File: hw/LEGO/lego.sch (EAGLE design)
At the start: 24 parts, among them IC1 ATMEGA48/88/168-AU

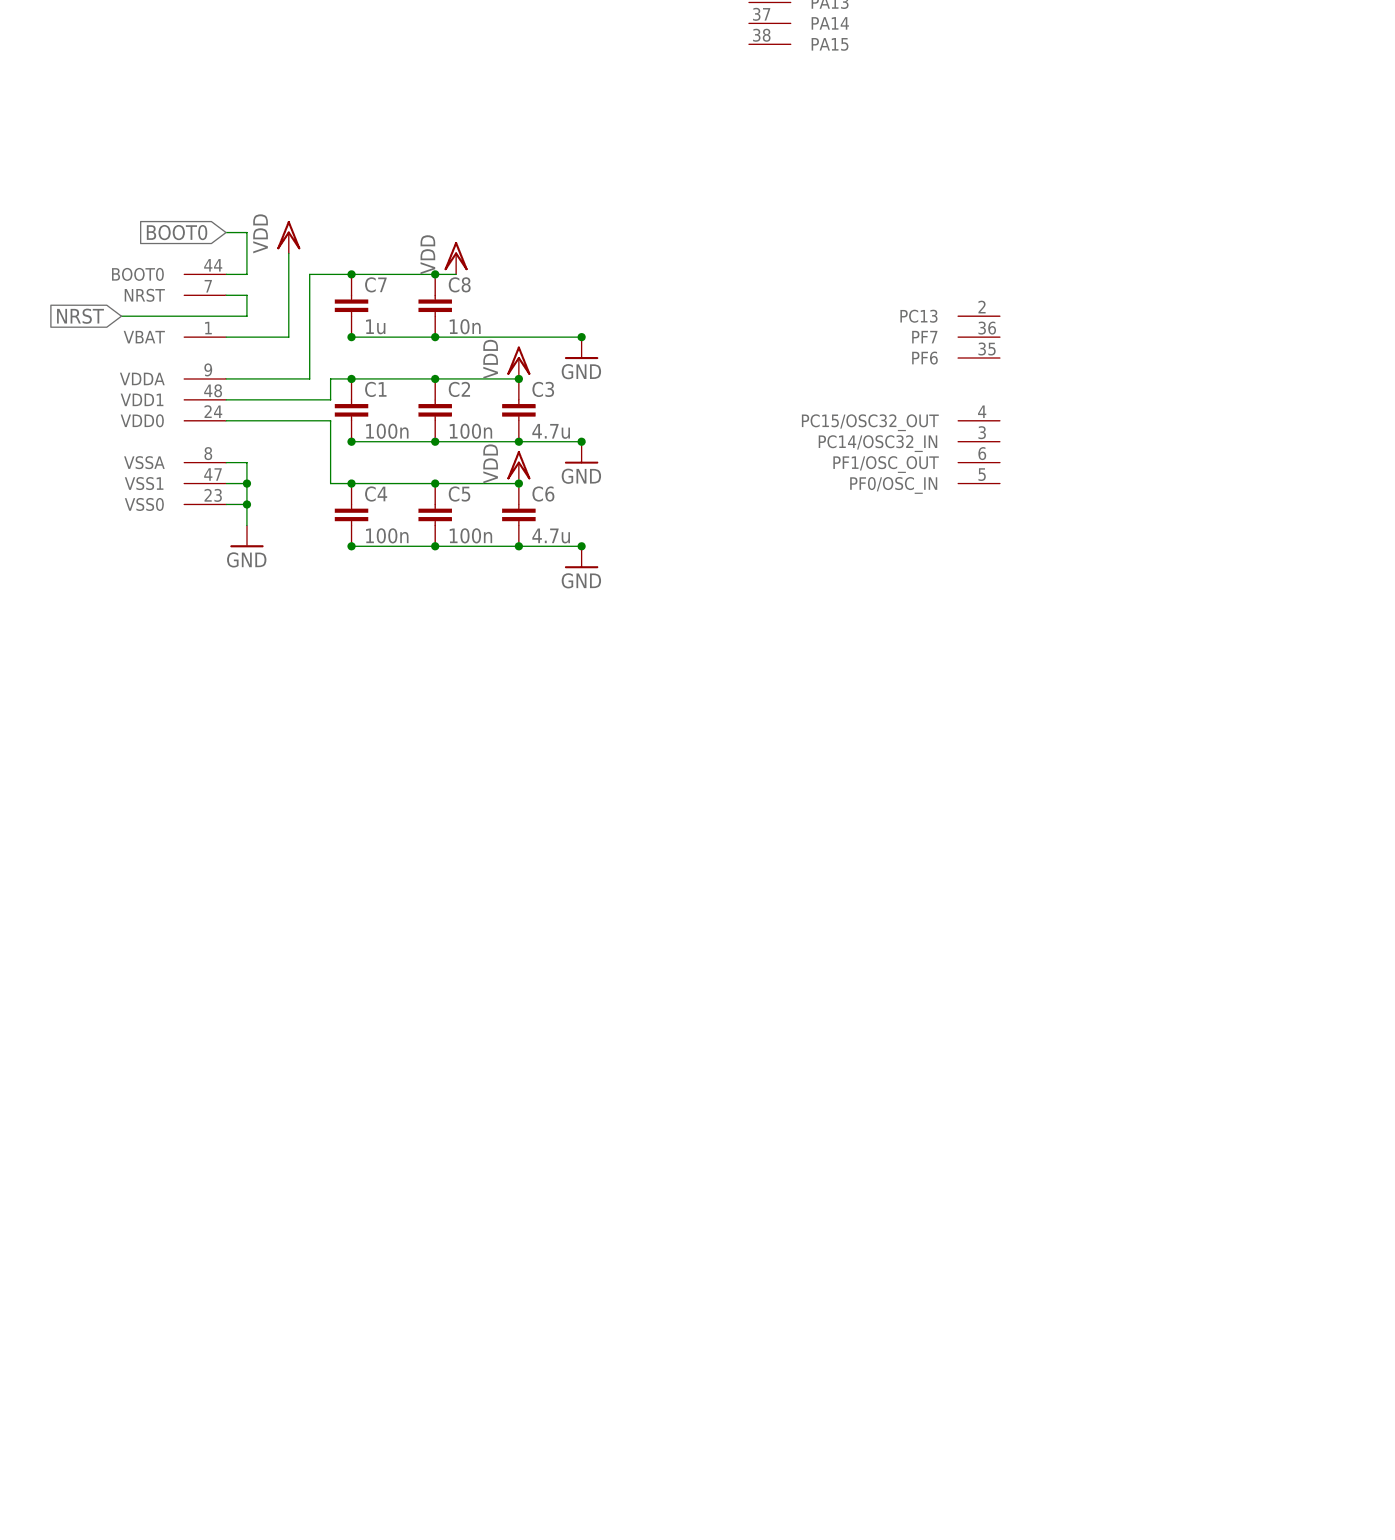
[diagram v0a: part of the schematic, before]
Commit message: Dodany układ mostka i kwarc do stm'a
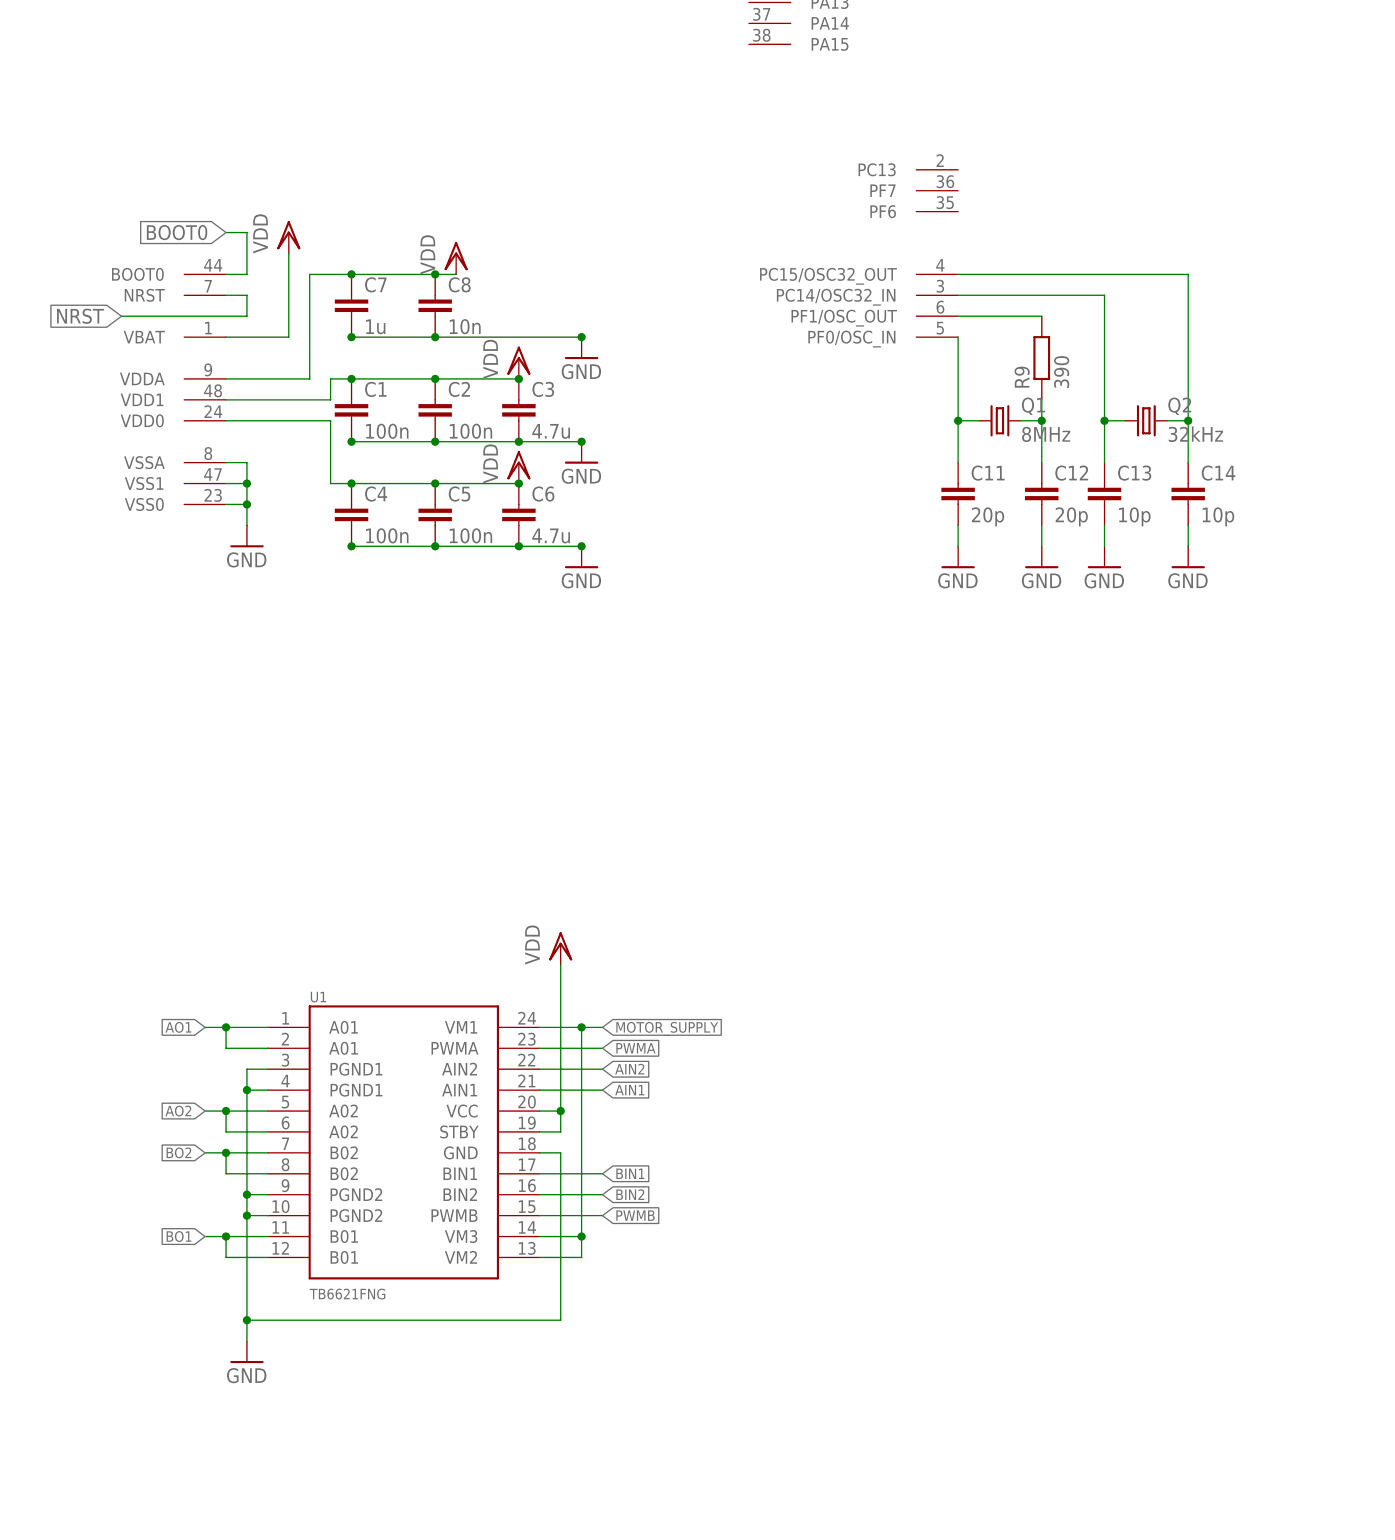
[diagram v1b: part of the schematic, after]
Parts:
- added C11, C12: 20p, rcl:C-EUC0805
- added C13, C14: 10p, rcl:C-EUC0805
- added Q1: 8MHz, crystal:CRYSTALHC49UP
- added Q2: 32kHz, crystal:CRYSTALHC49UP
- added R9: 390, rcl:R-EU_R0805
- added U1: TB6621FNG, SparkFun:TB6621FNG
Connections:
- new net AIN1: U1.AIN1
- new net AIN2: U1.AIN2
- new net AO1: U1.A01@1, U1.A01@2
- new net AO2: U1.A02@5, U1.A02@6
- new net BIN1: U1.BIN1
- new net BIN2: U1.BIN2
- new net BO1: U1.B01@11, U1.B01@12
- new net BO2: U1.B02@7, U1.B02@8
- new net MOTOR_SUPPLY: U1.VM1, U1.VM2, U1.VM3
- new net N$10: C12.1, Q1.2, R9.1
- new net N$11: C13.1, Q2.1, U$1G$4.PC14/OSC32_IN
- new net N$12: C14.1, Q2.2, U$1G$4.PC15/OSC32_OUT
- new net N$8: R9.2, U$1G$4.PF1/OSC_OUT
- new net N$9: C11.1, Q1.1, U$1G$4.PF0/OSC_IN
- new net PWMA: U1.PWMA
- new net PWMB: U1.PWMB
- net GND: now also C11.2, C12.2, C13.2, C14.2, U1.GND, U1.PGND1@3, U1.PGND1@4, U1.PGND2@10, U1.PGND2@9
- net VDD: now also U1.STBY, U1.VCC
